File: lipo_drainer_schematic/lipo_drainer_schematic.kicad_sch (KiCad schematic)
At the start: 59 parts, among them J1 BATT, J2 FAN, J3 Vcal, J4 128x64_OLED, J5 Gcal, J6 Ical, J7 Heatsink Temp (for MCP7901), Q1 MMBT3904, Q10 G700P06T, Q11 G700P06T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

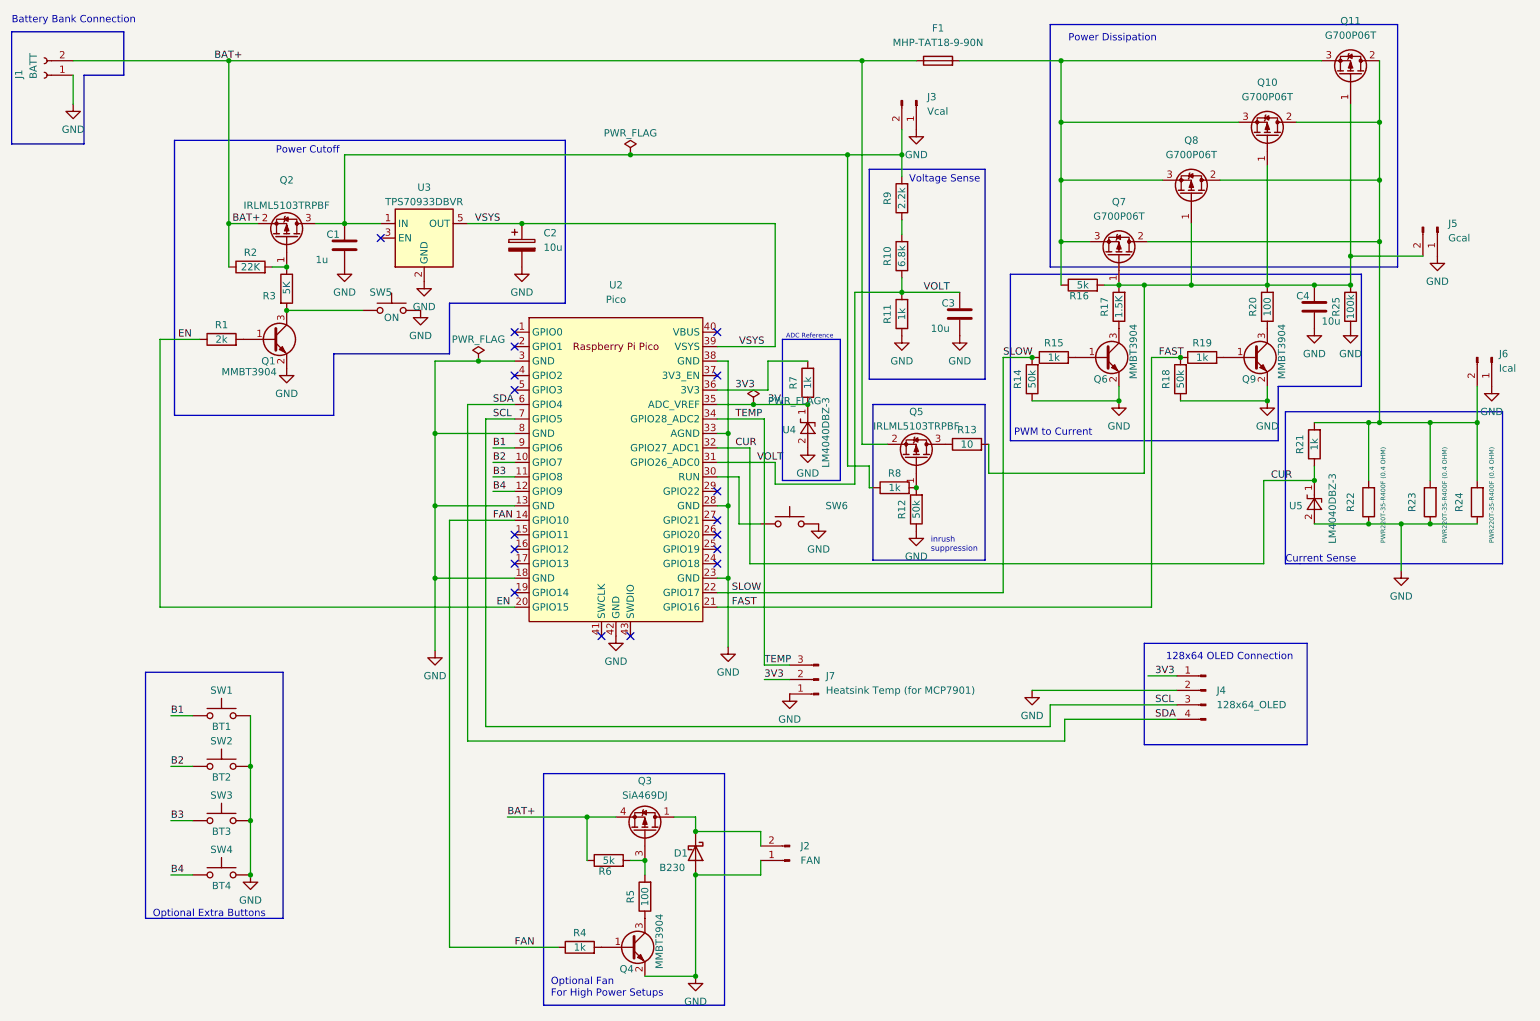
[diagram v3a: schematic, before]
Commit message: Added more net labels
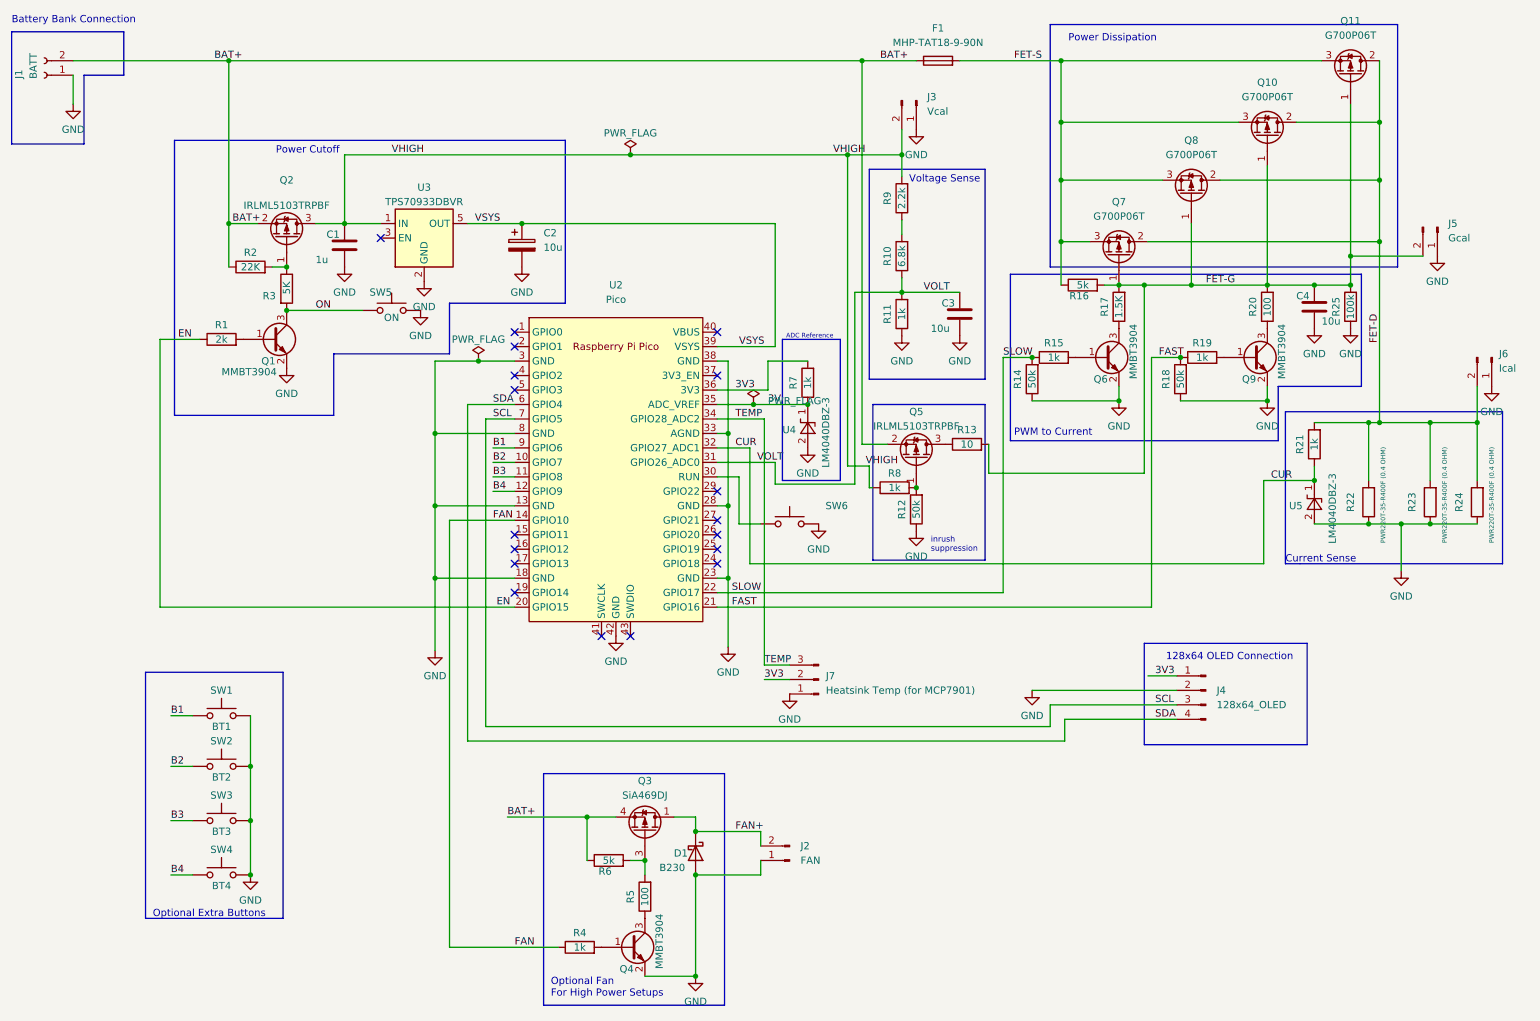
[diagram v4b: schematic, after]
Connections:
- net FET-G: now reaches C4.1, J5.2 (Pin_2), Q10.1 (G), Q11.1 (G), Q7.1 (G), Q8.1 (G), R13.2, R16.2, R17.2, R20.2, R25.2
- net FET-D: now reaches J6.2 (Pin_2), Q10.2 (D), Q11.2 (D), Q7.2 (D), Q8.2 (D), R21.2, R22.2, R23.2, R24.2
- net FET-S: now reaches F1.2, Q10.3 (S), Q11.3 (S), Q7.3 (S), Q8.3 (S), R16.1
- net VHIGH: now reaches C1.1, J3.2 (Pin_2), Q2.3 (D), R8.1, R9.2, U3.1 (IN)
- net FAN+: now reaches D1.1 (K), J2.2 (Pin_2), Q3.1 (D)
- net ON: now reaches Q1.3 (C), R3.2, SW5.1
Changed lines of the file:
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@@
+    (effects (font (size 1.27 1.27)) (justify left bottom))
+  )
+  (label "FET-G" (at 227.965 66.675 0) (fields_autoplaced)
     (effects (font (size 1.27 1.27)) (justify left bottom))
   )
@@
   )
   (label "VSYS" (at 146.05 77.47 0) (fields_autoplaced)
+    (effects (font (size 1.27 1.27)) (justify left bottom))
+  )
+  (label "VHIGH" (at 85.09 43.815 0) (fields_autoplaced)
+    (effects (font (size 1.27 1.27)) (justify left bottom))
+  )
+  (label "FET-S" (at 194.31 27.305 0) (fields_autoplaced)
     (effects (font (size 1.27 1.27)) (justify left bottom))
   )
@@
     (effects (font (size 1.27 1.27)) (justify left bottom))
   )
+  (label "VHIGH" (at 162.56 43.815 0) (fields_autoplaced)
+    (effects (font (size 1.27 1.27)) (justify left bottom))
+  )
   (label "CUR" (at 239.395 100.965 0) (fields_autoplaced)
     (effects (font (size 1.27 1.27)) (justify left bottom))
   )
   (label "FAN" (at 106.68 182.88 0) (fields_autoplaced)
+    (effects (font (size 1.27 1.27)) (justify left bottom))
+  )
+  (label "FET-D" (at 258.445 76.835 90) (fields_autoplaced)
     (effects (font (size 1.27 1.27)) (justify left bottom))
   )
@@
     (effects (font (size 1.27 1.27)) (justify left bottom))
   )
+  (label "VHIGH" (at 168.275 98.425 0) (fields_autoplaced)
+    (effects (font (size 1.27 1.27)) (justify left bottom))
+  )
+  (label "ON" (at 71.755 71.12 0) (fields_autoplaced)
+    (effects (font (size 1.27 1.27)) (justify left bottom))
+  )
   (label "CUR" (at 145.415 95.25 0) (fields_autoplaced)
     (effects (font (size 1.27 1.27)) (justify left bottom))
@@
     (effects (font (size 1.27 1.27)) (justify left bottom))
   )
+  (label "BAT+" (at 170.815 27.305 0) (fields_autoplaced)
+    (effects (font (size 1.27 1.27)) (justify left bottom))
+  )
   (label "3V3" (at 145.415 85.09 0) (fields_autoplaced)
     (effects (font (size 1.27 1.27)) (justify left bottom))
   )
+  (label "FAN+" (at 145.415 162.56 0) (fields_autoplaced)
+    (effects (font (size 1.27 1.27)) (justify left bottom))
+  )

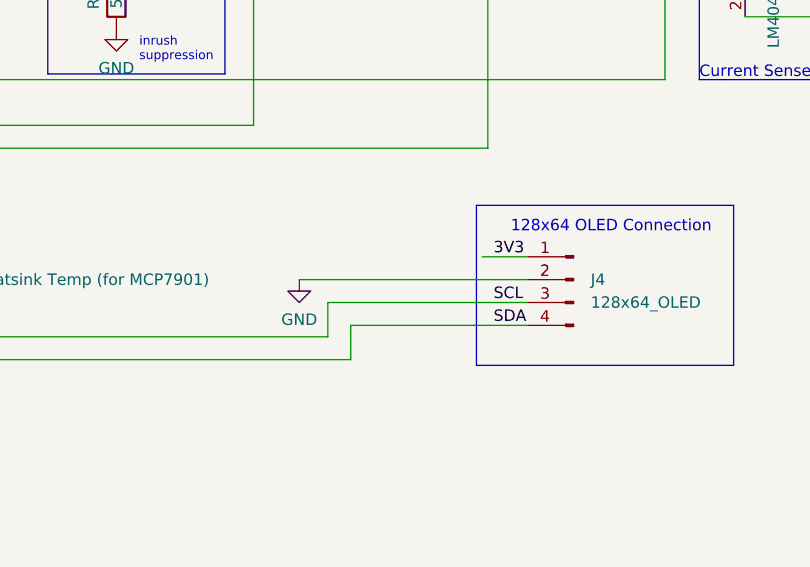
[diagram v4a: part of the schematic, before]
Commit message: Added OLED footprint
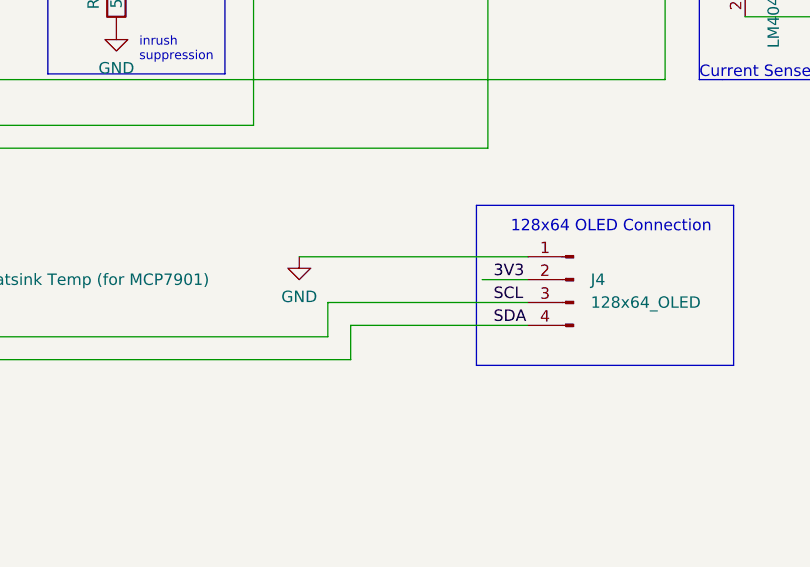
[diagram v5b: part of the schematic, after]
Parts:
- J4: footprint Connector_PinHeader_2.54mm:PinHeader_1x04_P2.54mm_Vertical -> Matt:OLED_128_64_1.3in
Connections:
- net 3V3: now also J4.2 (Pin_2); no longer J4.1 (Pin_1)
- net GND: now also J4.1 (Pin_1); no longer J4.2 (Pin_2)
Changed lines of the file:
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@@
     (stroke (width 0) (type default))
   )
-  (wire (pts (xy 197.485 137.795) (xy 222.885 137.795))
+  (wire (pts (xy 197.485 135.255) (xy 222.885 135.255))
     (stroke (width 0) (type default))
   )
@@
     (stroke (width 0) (type default))
   )
-  (wire (pts (xy 217.805 135.255) (xy 222.885 135.255))
+  (wire (pts (xy 217.805 137.795) (xy 222.885 137.795))
     (stroke (width 0) (type default))
   )
@@
     (effects (font (size 1.27 1.27)) (justify left bottom))
   )
-  (label "3V3" (at 219.075 135.255 0) (fields_autoplaced)
+  (label "3V3" (at 219.075 137.795 0) (fields_autoplaced)
     (effects (font (size 1.27 1.27)) (justify left bottom))
   )
@@
       (effects (font (size 1.27 1.27)) (justify right))
     )
-    (property "Footprint" "Connector_PinHeader_2.54mm:PinHeader_1x04_P2.54mm_Vertical" (at 227.965 137.795 0)
+    (property "Footprint" "Matt:OLED_128_64_1.3in" (at 227.965 137.795 0)
       (effects (font (size 1.27 1.27)) hide)
     )
@@
     )
   )
-  (symbol (lib_id "power:GND") (at 197.485 137.795 0) (unit 1)
-    (in_bom yes) (on_board yes) (dnp no) (fields_autoplaced)
-    (property "Reference" "#PWR019" (at 197.485 144.145 0)
-      (effects (font (size 1.27 1.27)) hide)
-    )
-    (property "Value" "GND" (at 197.485 142.24 0)
-      (effects (font (size 1.27 1.27)))
-    )
-    (property "Footprint" "" (at 197.485 137.795 0)
-      (effects (font (size 1.27 1.27)) hide)
-    )
-    (property "Datasheet" "" (at 197.485 137.795 0)
-      (effects (font (size 1.27 1.27)) hide)
-    )
+  (symbol (lib_id "power:GND") (at 197.485 135.255 0) (unit 1)
+    (in_bom yes) (on_board yes) (dnp no) (fields_autoplaced)
+    (property "Reference" "#PWR019" (at 197.485 141.605 0)
+      (effects (font (size 1.27 1.27)) hide)
+    )
+    (property "Value" "GND" (at 197.485 139.7 0)
+      (effects (font (size 1.27 1.27)))
+    )
+    (property "Footprint" "" (at 197.485 135.255 0)
+      (effects (font (size 1.27 1.27)) hide)
+    )
+    (property "Datasheet" "" (at 197.485 135.255 0)
+      (effects (font (size 1.27 1.27)) hide)
+    )

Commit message: Change XT-60 connecter
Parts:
- J1: footprint Connector_AMASS:AMASS_XT60-M_1x02_P7.20mm_Vertical -> Connector_AMASS:AMASS_XT60PW-M_1x02_P7.20mm_Horizontal
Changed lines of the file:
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@@
       (effects (font (size 1.27 1.27)) (justify right))
     )
-    (property "Footprint" "Connector_AMASS:AMASS_XT60-M_1x02_P7.20mm_Vertical" (at 24.13 29.845 0)
+    (property "Footprint" "Connector_AMASS:AMASS_XT60PW-M_1x02_P7.20mm_Horizontal" (at 24.13 29.845 0)
       (effects (font (size 1.27 1.27)) hide)
     )

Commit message: Changed button definitions.
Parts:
- removed SW4: BT4, Matt:SMD_Button_6mm_3_5mm, symbol Switch:SW_Push
- SW1: value BT1 -> OFF
- SW2: value BT2 -> NEXT
- SW3: value BT3 -> OK
- renumbered SW6 to SW4
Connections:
- net B1 renamed OFF
- net B2 renamed NEXT
- net B3 renamed OK
- net B4: no longer names the net of U2.12 (GPIO9)
- no-connect marks 18 -> 19
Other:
- note added: "Control Buttons"
- note removed: "Optional Extra Buttons"

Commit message: Routed and added mounting holes.
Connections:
- net EN: now also U2.27 (GPIO21); no longer U2.20 (GPIO15)
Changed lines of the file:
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@@
   (no_connect (at 106.68 110.49))
   (no_connect (at 142.24 110.49))
+  (no_connect (at 106.68 123.19))
   (no_connect (at 106.68 77.47))
-  (no_connect (at 142.24 107.95))
   (no_connect (at 83.185 58.42))
   (no_connect (at 142.24 102.87))
@@
     (stroke (width 0) (type default))
   )
-  (wire (pts (xy 44.45 76.2) (xy 44.45 123.19))
-    (stroke (width 0) (type default))
-  )
   (polyline (pts (xy 74.93 89.535) (xy 46.99 89.535))
     (stroke (width 0) (type default))
@@
     (stroke (width 0) (type default))
   )
+  (wire (pts (xy 145.415 107.95) (xy 145.415 113.03))
+    (stroke (width 0) (type default))
+  )
   (wire (pts (xy 138.43 162.56) (xy 149.86 162.56))
     (stroke (width 0) (type default))
@@
     (stroke (width 0) (type default))
   )
-  (wire (pts (xy 44.45 123.19) (xy 106.68 123.19))
-    (stroke (width 0) (type default))
-  )
   (wire (pts (xy 202.565 48.26) (xy 220.345 48.26))
     (stroke (width 0) (type default))
@@
   )
   (wire (pts (xy 76.835 55.88) (xy 76.835 43.815))
+    (stroke (width 0) (type default))
+  )
+  (wire (pts (xy 142.24 107.95) (xy 145.415 107.95))
     (stroke (width 0) (type default))
   )
@@
     (effects (font (size 1.27 1.27)) (justify left bottom))
   )
+  (label "EN" (at 145.415 113.03 0) (fields_autoplaced)
+    (effects (font (size 1.27 1.27)) (justify left bottom))
+  )
   (label "SDA" (at 102.87 87.63 0) (fields_autoplaced)
     (effects (font (size 1.27 1.27)) (justify left bottom))
@@
     (effects (font (size 1.27 1.27)) (justify left bottom))
   )
-  (label "EN" (at 103.505 123.19 0) (fields_autoplaced)
-    (effects (font (size 1.27 1.27)) (justify left bottom))
-  )
